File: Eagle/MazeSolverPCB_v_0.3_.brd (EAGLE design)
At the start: 53.3 x 50.8 mm, 26 parts

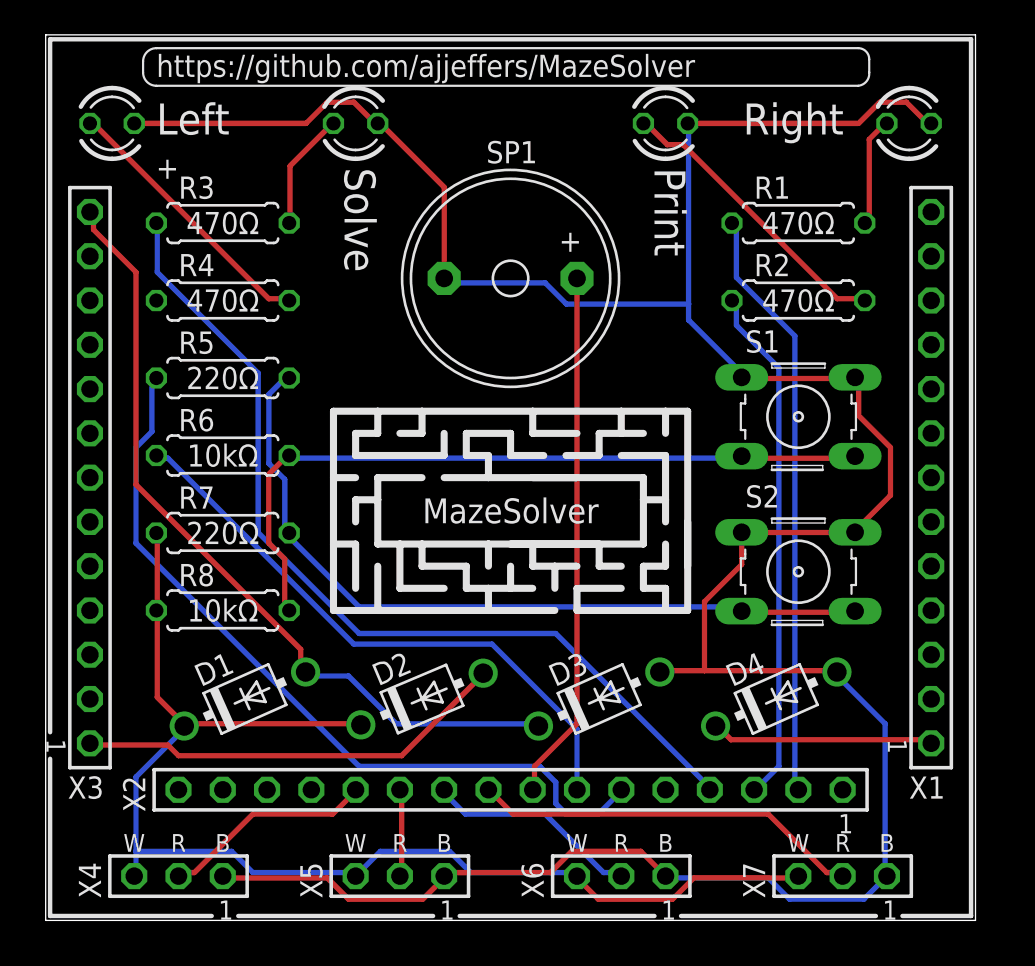
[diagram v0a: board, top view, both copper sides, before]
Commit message: Fixed Eagle routing.
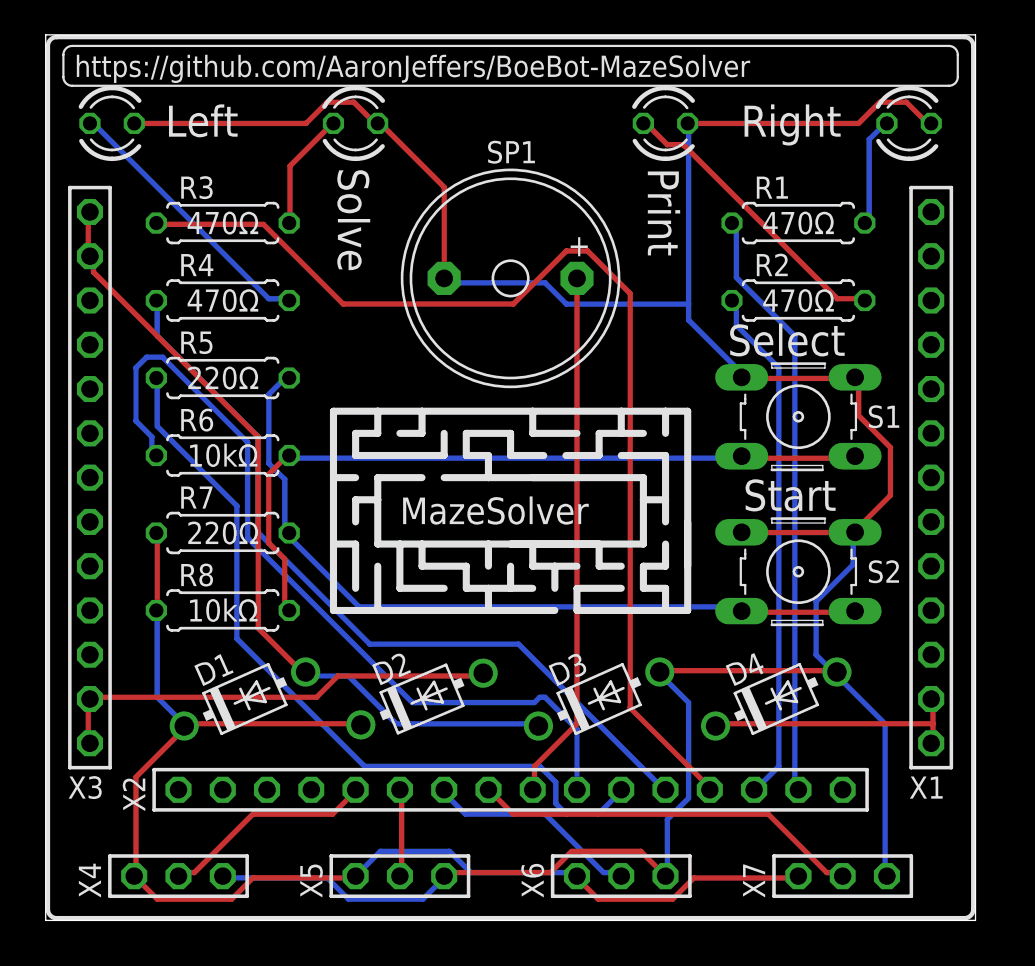
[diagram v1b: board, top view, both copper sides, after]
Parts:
- X1, X3: device con-samtec:TSW-113-02-S-S -> aaron:TSW-113-02-S-S
- X2: device con-samtec:TSW-116-02-S-S -> aaron:TSW-116-02-S-S
- X4, X5, X6, X7: device con-samtec:TSW-103-02-S-S -> aaron:TSW-103-02-S-S
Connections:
- removed net N$16: X2.16
- removed net N$18: X3.10
- removed net N$22: X1.13
- removed net N$23: X3.11
- removed net N$24: D2.A, X3.1
- removed net N$31: X2.15
- removed net N$6 (its old number): X2.1
- removed net N$9 (its old number): R4.1
- new net N$15: D2.A, X3.1, X3.2
- net N$20: now also X3.12
- net N$25: now also R4.1
- net N$8: now also X1.2
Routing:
- net N$25: track 0.00 -> 45.2 mm
- net N$15: track 0.00 -> 25.8 mm
- net N$24: track 24.8 -> 0.00 mm
- net N$27: track 34.2 -> 46.9 mm
- net N$6: track 52.3 -> 61.8 mm
- net N$8: track 12.8 -> 15.1 mm
- net N$26: track 45.7 -> 44.4 mm
- net N$2: track 72.7 -> 73.3 mm
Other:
- board text added: "For Parallax BOE and BOE Shield"
- board text added: "Select"
- board text added: "Start"
- board text added: "https://github.com/AaronJeffers/BoeBot-MazeSolver"
- board text removed: "B"
- board text removed: "For Parallax BOE and BOE Shield."
- board text removed: "R"
- board text removed: "W"
- board text removed: "https://github.com/ajjeffers/MazeSolver"
